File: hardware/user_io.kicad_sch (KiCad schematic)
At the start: 6 parts

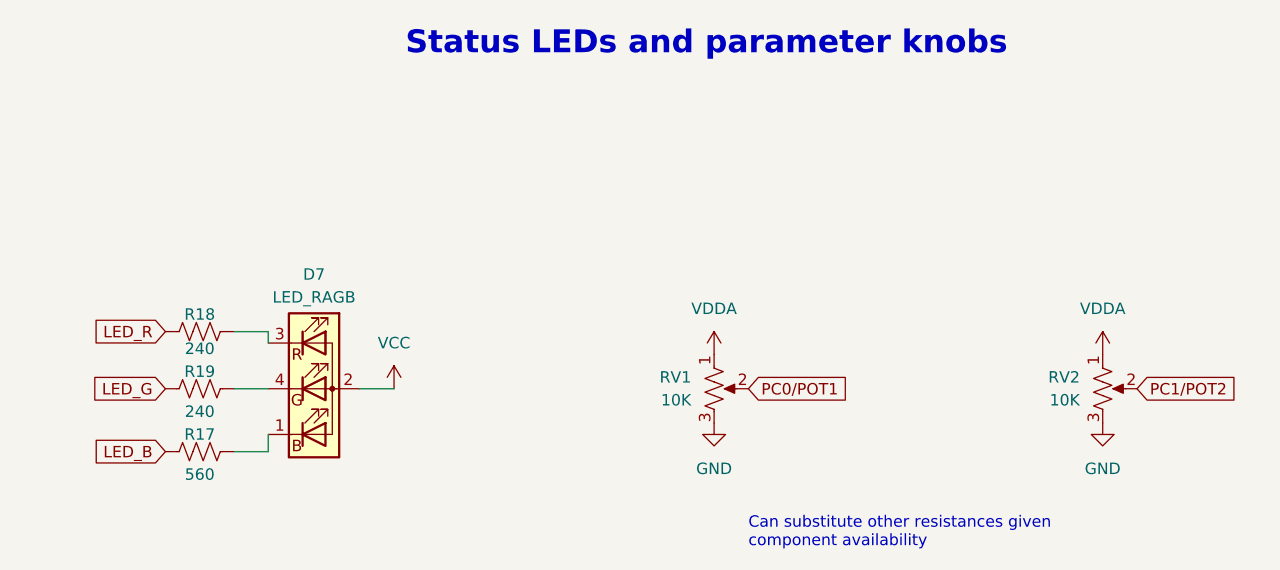
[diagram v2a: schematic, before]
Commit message: use nucleo 3.3v vdda; add 2nd low-pass stage to input
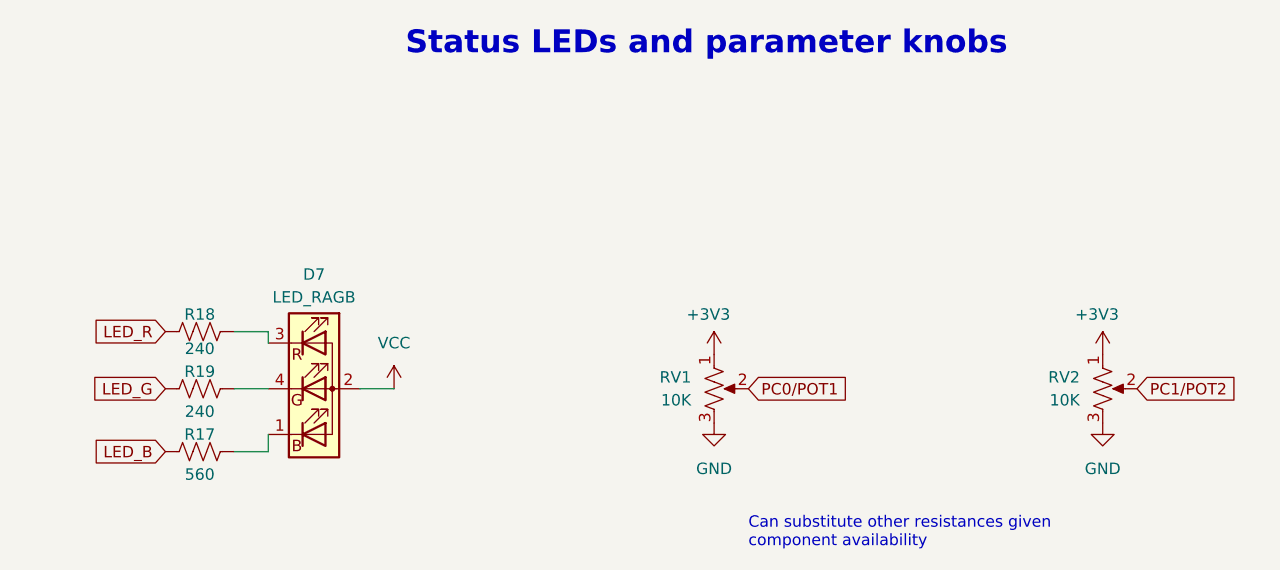
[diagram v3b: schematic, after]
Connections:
- net VDDA renamed +3V3
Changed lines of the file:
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@@
   (title_block
     (title "DSP PAW add-on board")
-    (date "2023-09-04")
+    (date "2023-09-13")
     (rev "2")
     (company "bitgloo")
@@
     )
   )
-  (symbol (lib_id "power:VDDA") (at 193.04 102.87 0) (unit 1)
-    (in_bom yes) (on_board yes) (dnp no) (fields_autoplaced)
-    (property "Reference" "#PWR013" (at 193.04 106.68 0)
-      (effects (font (size 1.27 1.27)) hide)
-    )
-    (property "Value" "VDDA" (at 193.04 97.79 0)
-      (effects (font (size 1.27 1.27)))
-    )
-    (property "Footprint" "" (at 193.04 102.87 0)
-      (effects (font (size 1.27 1.27)) hide)
-    )
-    (property "Datasheet" "" (at 193.04 102.87 0)
-      (effects (font (size 1.27 1.27)) hide)
-    )
-    (pin "1")
-    (instances
-      (project "stmdsp_rev3"
-        (path "/975c3983-57e7-4e06-a697-831e5209dd80"
-          (reference "#PWR013") (unit 1)
-        )
-      )
-      (project "DSP PAW add-on board"
-        (path "/c291319b-d76e-4fda-91cc-061acff65f9f/270d19d2-3af2-41db-ad1c-33373417ec82"
-          (reference "#PWR033") (unit 1)
-        )
-        (path "/c291319b-d76e-4fda-91cc-061acff65f9f/97fc232a-dbc7-49da-a6a0-e33e9aacbabd"
-          (reference "#PWR024") (unit 1)
-        )
-        (path "/c291319b-d76e-4fda-91cc-061acff65f9f/7798c5d5-f9b1-4b2e-811c-a15abcd34bfa"
-          (reference "#PWR067") (unit 1)
-        )
-      )
-    )
-  )
   (symbol (lib_id "power:GND") (at 193.04 110.49 0) (unit 1)
     (in_bom yes) (on_board yes) (dnp no) (fields_autoplaced)
@@
     )
   )
+  (symbol (lib_id "power:+3V3") (at 149.86 102.87 0) (unit 1)
+    (in_bom yes) (on_board yes) (dnp no)
+    (property "Reference" "#PWR024" (at 149.86 106.68 0)
+      (effects (font (size 1.27 1.27)) hide)
+    )
+    (property "Value" "+3V3" (at 149.225 98.425 0)
+      (effects (font (size 1.27 1.27)))
+    )
+    (property "Footprint" "" (at 149.86 102.87 0)
+      (effects (font (size 1.27 1.27)) hide)
+    )
+    (property "Datasheet" "" (at 149.86 102.87 0)
+      (effects (font (size 1.27 1.27)) hide)
+    )
+    (pin "1")
+    (instances
+      (project "DSP PAW add-on board"
+        (path "/c291319b-d76e-4fda-91cc-061acff65f9f/97fc232a-dbc7-49da-a6a0-e33e9aacbabd"
+          (reference "#PWR024") (unit 1)
+        )
+        (path "/c291319b-d76e-4fda-91cc-061acff65f9f/7798c5d5-f9b1-4b2e-811c-a15abcd34bfa"
+          (reference "#PWR077") (unit 1)
+        )
+      )
+    )
+  )
   (symbol (lib_id "Device:LED_BARG") (at 105.41 106.68 0) (unit 1)
     (in_bom yes) (on_board yes) (dnp no) (fields_autoplaced)
@@
     )
   )
-  (symbol (lib_id "power:VDDA") (at 149.86 102.87 0) (unit 1)
-    (in_bom yes) (on_board yes) (dnp no) (fields_autoplaced)
-    (property "Reference" "#PWR013" (at 149.86 106.68 0)
-      (effects (font (size 1.27 1.27)) hide)
-    )
-    (property "Value" "VDDA" (at 149.86 97.79 0)
-      (effects (font (size 1.27 1.27)))
-    )
-    (property "Footprint" "" (at 149.86 102.87 0)
-      (effects (font (size 1.27 1.27)) hide)
-    )
-    (property "Datasheet" "" (at 149.86 102.87 0)
-      (effects (font (size 1.27 1.27)) hide)
-    )
-    (pin "1")
-    (instances
-      (project "stmdsp_rev3"
-        (path "/975c3983-57e7-4e06-a697-831e5209dd80"
-          (reference "#PWR013") (unit 1)
-        )
-      )
-      (project "DSP PAW add-on board"
-        (path "/c291319b-d76e-4fda-91cc-061acff65f9f/270d19d2-3af2-41db-ad1c-33373417ec82"
-          (reference "#PWR033") (unit 1)
-        )
+  (symbol (lib_id "power:+3V3") (at 193.04 102.87 0) (unit 1)
+    (in_bom yes) (on_board yes) (dnp no)
+    (property "Reference" "#PWR024" (at 193.04 106.68 0)
+      (effects (font (size 1.27 1.27)) hide)
+    )
+    (property "Value" "+3V3" (at 192.405 98.425 0)
+      (effects (font (size 1.27 1.27)))
+    )
+    (property "Footprint" "" (at 193.04 102.87 0)
+      (effects (font (size 1.27 1.27)) hide)
+    )
+    (property "Datasheet" "" (at 193.04 102.87 0)
+      (effects (font (size 1.27 1.27)) hide)
+    )
+    (pin "1")
+    (instances
+      (project "DSP PAW add-on board"
         (path "/c291319b-d76e-4fda-91cc-061acff65f9f/97fc232a-dbc7-49da-a6a0-e33e9aacbabd"
           (reference "#PWR024") (unit 1)
         )
         (path "/c291319b-d76e-4fda-91cc-061acff65f9f/7798c5d5-f9b1-4b2e-811c-a15abcd34bfa"
-          (reference "#PWR054") (unit 1)
-        )
-      )
+          (reference "#PWR078") (unit 1)
+        )
+      )
